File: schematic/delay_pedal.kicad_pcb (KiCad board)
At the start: 4 copper layers, 110 x 50 mm, 140 parts, among them J1 IN Gain, J10 VFLASH, J12 LP, J13 Mix, J14 OUT Gain, J3 SPI FLASH, J4 Audio In, J5 FDBK, J6 +9V, J8 Time, J9 Audio Out, SW1 RESET, SW2 SW_SPST, U1 ICE40LP1K-QN84, U10 TPL810ADJ-5TR, U11 TPL810F50-89TR, U12 ADS8339IDGSR, U13 TLV76033DBZR, U14 OPA1678, U15 DAC8551IADGKR, U16 REF5045AD, U17 OPA1678, U2 APS1604M-3SQR, U3 OPA1678, U4 NXB0104, U5 OPA1678, U6 W25X20CLSN, U8 OPA1678, U9 OPA1678, X1 KXO-V96T

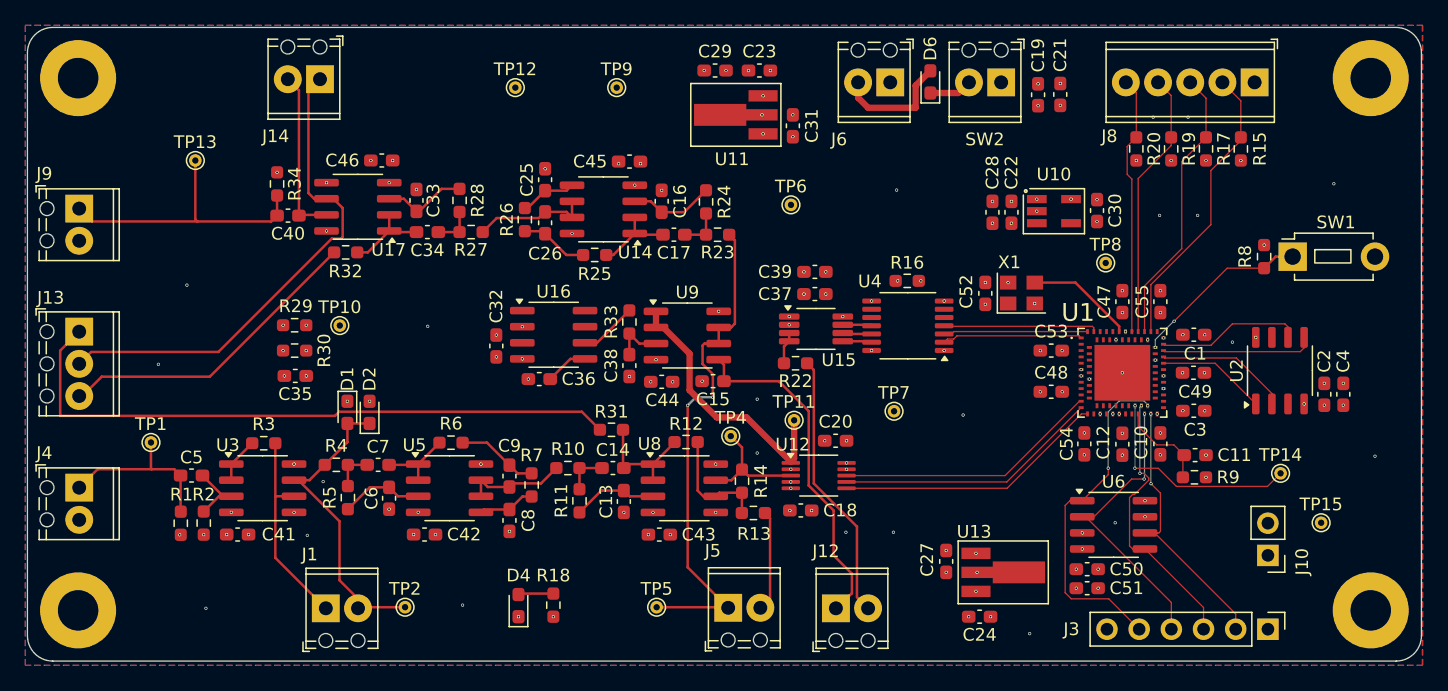
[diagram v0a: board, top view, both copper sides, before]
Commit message: Added missing capacitors to analog signal chain
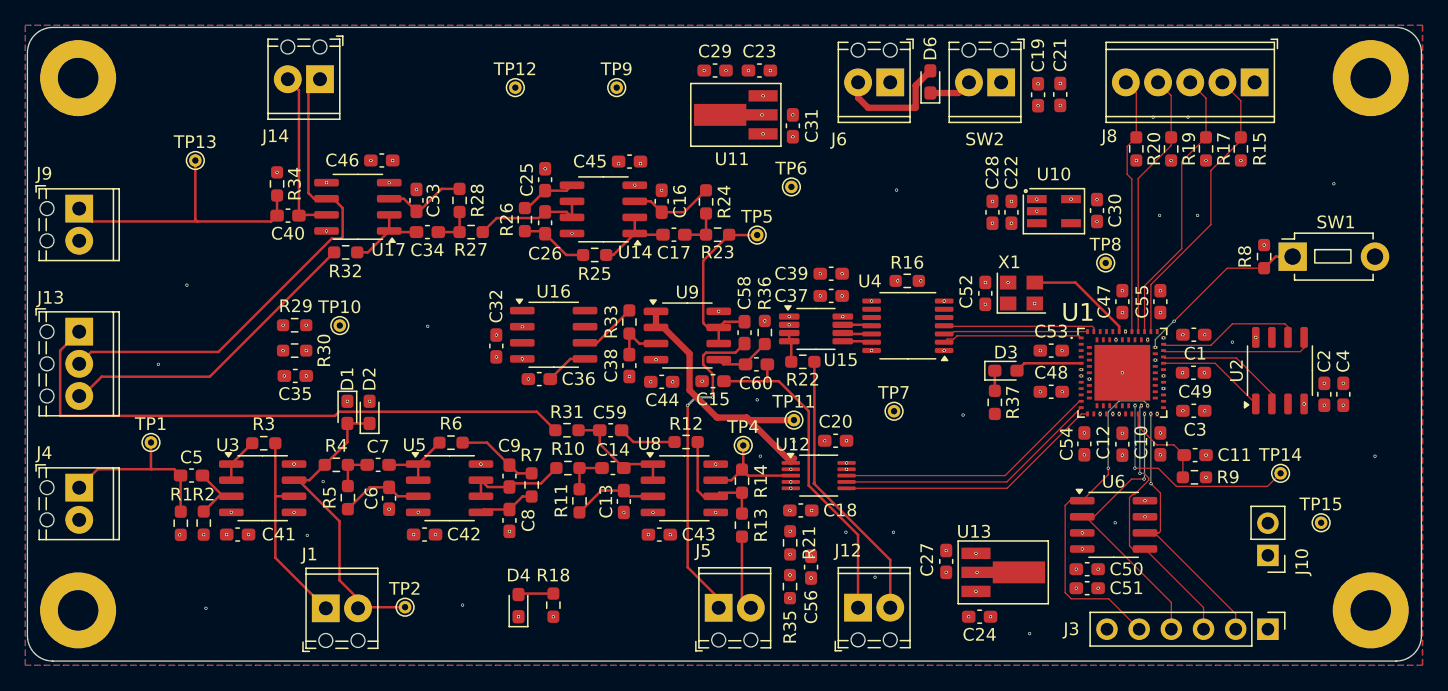
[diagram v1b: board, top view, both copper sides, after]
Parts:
- added C56: 47u, Capacitor_SMD:C_0603_1608Metric_Pad1.08x0.95mm_HandSolder, F.Cu at (156.8, 117.5)
- added C58: 0.47u, Capacitor_SMD:C_0603_1608Metric_Pad1.08x0.95mm_HandSolder, F.Cu at (151.5, 99.0)
- added C59: 0.47u, Capacitor_SMD:C_0603_1608Metric_Pad1.08x0.95mm_HandSolder, F.Cu at (140.9, 106.7)
- added C60: 0.1u, Capacitor_SMD:C_0603_1608Metric_Pad1.08x0.95mm_HandSolder, F.Cu at (152.4, 101.5)
- added D3: LED, LED_SMD:LED_0603_1608Metric_Pad1.05x0.95mm_HandSolder, F.Cu at (172.1, 102.0)
- added R21: 40k, Resistor_SMD:R_0603_1608Metric_Pad0.98x0.95mm_HandSolder, F.Cu at (155.1, 115.6)
- added R35: 40k, Resistor_SMD:R_0603_1608Metric_Pad0.98x0.95mm_HandSolder, F.Cu at (155.1, 119.0)
- added R36: 1M, Resistor_SMD:R_0603_1608Metric_Pad0.98x0.95mm_HandSolder, F.Cu at (153.1, 99.0)
- added R37: 1k, Resistor_SMD:R_0603_1608Metric_Pad0.98x0.95mm_HandSolder, F.Cu at (171.2, 104.5)
- R12, R13, R14, R31, R32: value 10k -> 20k
- R29, R30: value 10k -> 40k
- moved TP5 30.4 mm to (152.5, 91.3)
- moved R31 3.51 mm to (137.5, 106.7)
- moved J12 1.75 mm to (160.5, 120.7)
- moved TP6 1.41 mm to (155.2, 87.5)
- moved R13 1.32 mm to (151.3, 114.2), turned to -90 degrees
- moved C37 1.29 mm to (158.3, 96.1)
- moved C39 1.29 mm to (158.3, 94.3)
- moved TP4 1.23 mm to (151.4, 107.9)
- moved J5 0.75 mm to (149.5, 120.7)
- moved R22 0.58 mm to (156.1, 101.3)
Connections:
- R12 pad 1: Net-(U8A--) -> Net-(C59-Pad1)
- R23 pad 2: Net-(J5-Pin_1) -> Net-(U9B--)
- TP5 pad 1: Net-(J5-Pin_1) -> Net-(U9B--)
- U1 pad A5: unconnected-(U1-IOL_5B-PadA5) -> /ICELED
- U8 pad 5: Vref -> +2V5
- U9 pad 5: Net-(J12-Pin_1) -> Net-(U9B-+)
- U9 pad 6: Net-(J5-Pin_1) -> Net-(U9B--)
- U9 pad 7: Net-(J5-Pin_1) -> Net-(U9B--)
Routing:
- net Net-(U9B--): track 0.00 -> 15.4 mm
- net Net-(J5-Pin_1): track 40.7 -> 26.5 mm
- net /ICELED: track 0.00 -> 5.31 mm
- net Net-(C59-Pad1): track 0.00 -> 4.61 mm
- net Net-(U9B-+): track 0.00 -> 4.50 mm
- net Net-(J13-Pin_1): track 50.6 -> 47.1 mm
- net Net-(D3-K): track 0.00 -> 1.59 mm
- net /VADC: track 9.48 -> 8.41 mm
- net Aref: track 21.4 -> 22.2 mm
- net Net-(J5-Pin_2): track 8.03 -> 7.38 mm
- net Net-(J12-Pin_1): track 26.9 -> 27.5 mm
- net +2V5: track 0.00 -> 0.02 mm, vias 0 -> 4
- net GND: vias 96 -> 100
- net +5V: vias 11 -> 12
- added copper zone on In2.Cu, net +2V5
